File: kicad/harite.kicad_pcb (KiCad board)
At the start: 2 copper layers, 8 parts, among them J1 503480-0500, U3 Raspberry_Pi_Pico

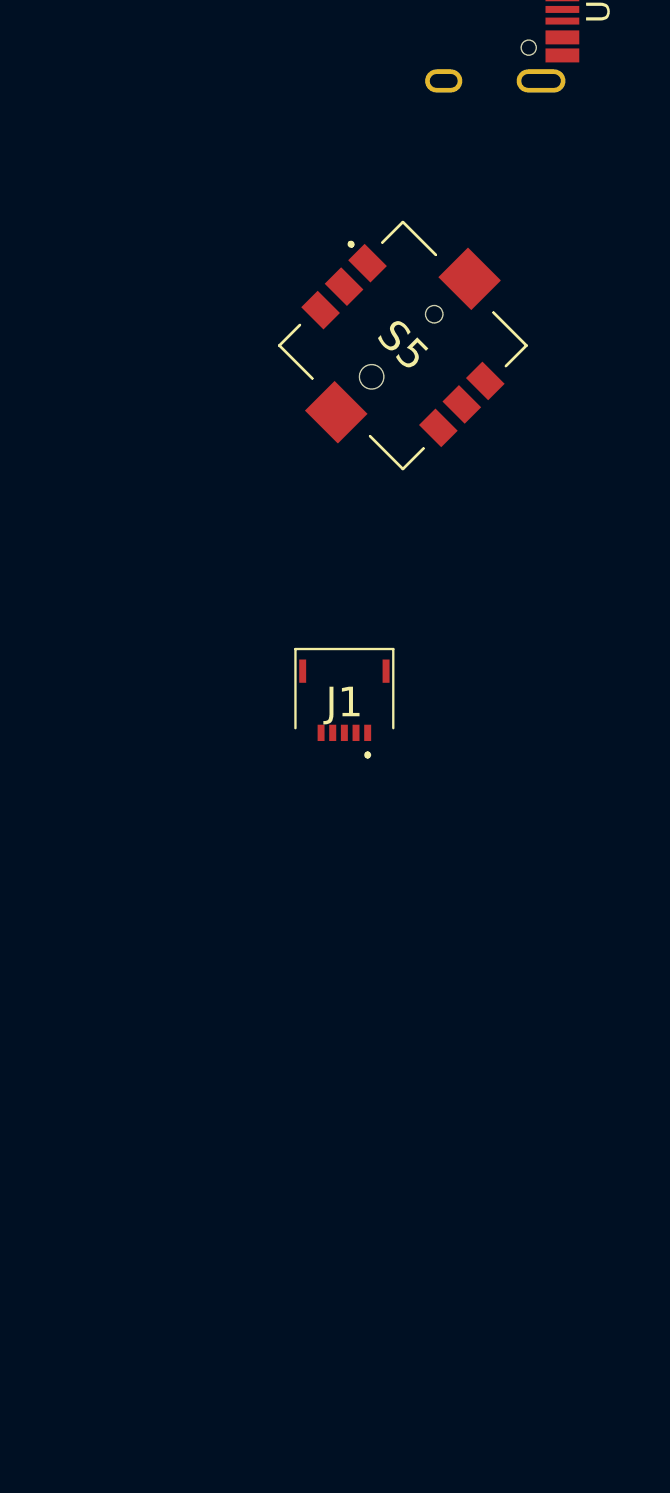
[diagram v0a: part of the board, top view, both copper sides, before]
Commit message: Add 5034800540 and 5034801000
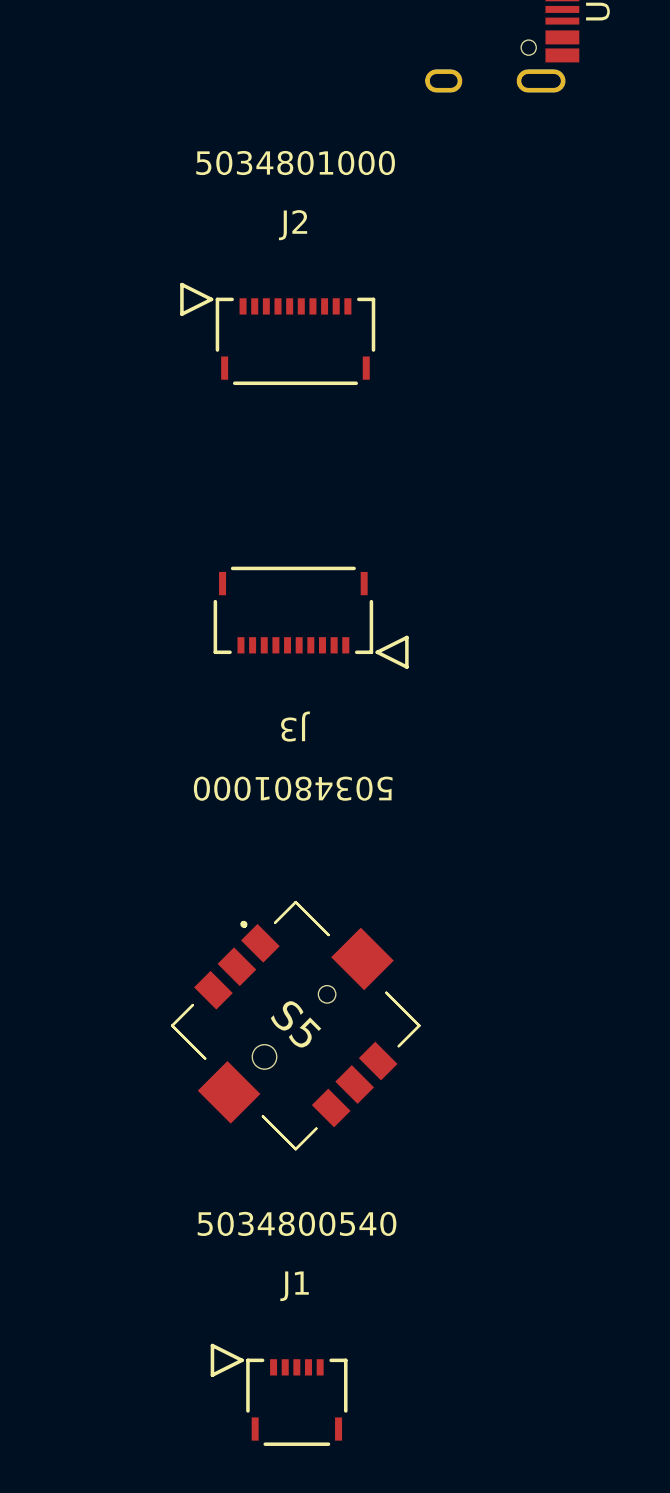
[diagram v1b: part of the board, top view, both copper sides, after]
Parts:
- added J2: 5034801000, footprints:5034801000, F.Cu at (99.2, 120.2)
- added J3: 5034801000, footprints:5034801000, F.Cu at (99.2, 131.8)
- J1: footprint footprints:5034800500 -> footprints:5034800540
- S1, S2, S3, S4, S5: footprint footprints:SKRHADE -> footprints:SKRHADE010
- moved J1 30.4 mm to (99.3, 165.8), turned to 0 degrees
- moved S5 29.6 mm to (99.3, 149.6)
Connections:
- J1 pad 1: 3V3 -> EJX
- J1 pad 2: JY -> EGND
- J1 pad 3: JC -> EJC
- J1 pad 4: GND -> EJY
- J1 pad 5: JX -> E3V3
- S5 pad 1: TN -> ETN
- S5 pad 2: TC -> ETC
- S5 pad 3: TW -> ETW
- S5 pad 4: TE -> ETE
- S5 pad 5: GND -> EGND
- S5 pad 6: TS -> ETS

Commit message: Fix model
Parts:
- J2, J3: value 5034801000 -> CON_5034801000_MOL
- moved USB1 19.4 mm to (122.4, 105.2), turned to 90 degrees
- moved J2 12.8 mm to (100.7, 107.5)
- moved J1 6.85 mm to (99.2, 158.9)
- moved U3 4.10 mm to (47.2, 119.4)
- moved S5 4.00 mm to (99.1, 145.6)
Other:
- board outline added: 100.1 x 93.3 mm

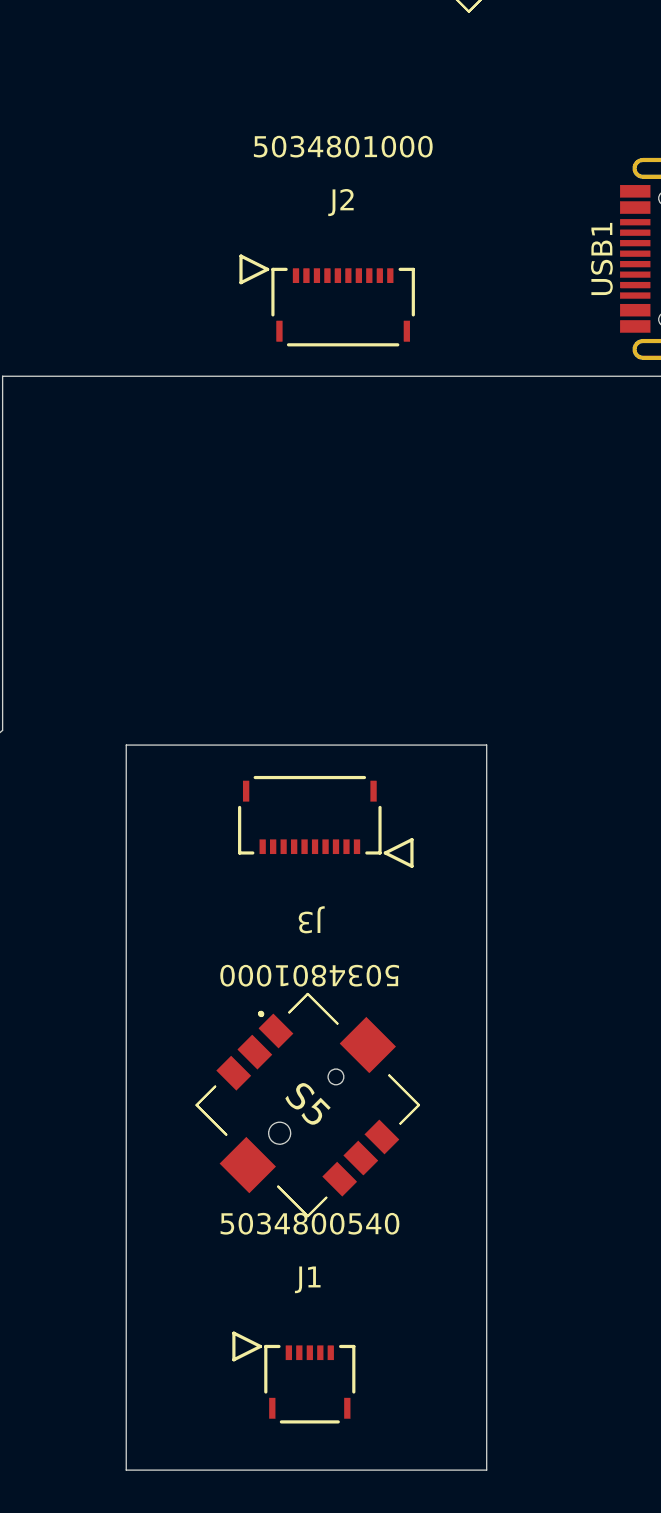
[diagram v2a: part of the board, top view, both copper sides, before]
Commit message: fix orientation
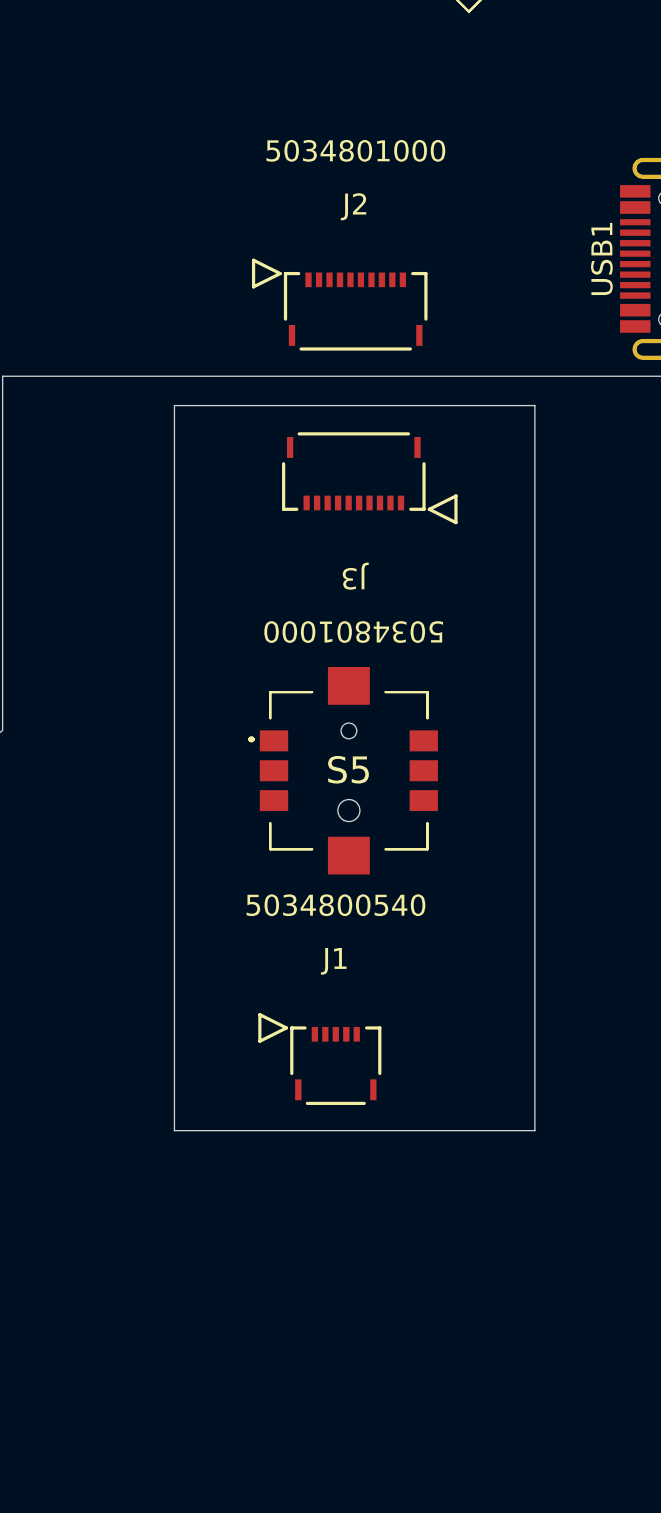
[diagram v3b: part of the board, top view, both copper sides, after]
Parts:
- J2, J3: value CON_5034801000_MOL -> 5034801000
- moved J3 16.5 mm to (101.3, 115.3)
- moved S5 16.1 mm to (101.0, 129.6), turned to 0 degrees
- moved J1 15.3 mm to (100.4, 143.7)
- moved J2 0.63 mm to (101.3, 107.7)
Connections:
- J1 pad 1: EJX -> E3V3
- J1 pad 2: EGND -> EJY
- J1 pad 4: EJY -> EGND
- J1 pad 5: E3V3 -> EJX
- J2 pad 10: GND -> TS
- J2 pad 4: JX -> GND
- J2 pad 5: TS -> JX
- J2 pad 6: TE -> TN
- J2 pad 7: TC -> TW
- J2 pad 8: TW -> TC
- J2 pad 9: TN -> TE
- J3 pad 1: EGND -> ETS
- J3 pad 2: ETN -> ETE
- J3 pad 3: ETW -> ETC
- J3 pad 4: ETC -> ETW
- J3 pad 5: ETE -> ETN
- J3 pad 6: ETS -> EJX
- J3 pad 7: EJX -> EGND
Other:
- board size 100.1 x 93.3 mm -> 100.1 x 77.1 mm

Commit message: update
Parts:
- added REF**: MountingHole_2.2mm_M2_Pad_Via, MountingHole:MountingHole_2.2mm_M2_Pad_Via, F.Cu at (68.5, 75.9)
- added REF**: MountingHole_2.2mm_M2_Pad_Via, MountingHole:MountingHole_2.2mm_M2_Pad_Via, F.Cu at (113.0, 96.2)
- added REF**: MountingHole_2.2mm_M2_Pad_Via, MountingHole:MountingHole_2.2mm_M2_Pad_Via, F.Cu at (80.0, 127.1)
- added REF**: MountingHole_2.2mm_M2_Pad_Via, MountingHole:MountingHole_2.2mm_M2_Pad_Via, F.Cu at (24.2, 102.6)
- moved J1 6.34 mm to (101.1, 137.4)
- moved S5 3.26 mm to (101.0, 126.4), turned to -45 degrees
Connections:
- S1 pad 2: unconnected-(S1-CENTER-Pad2) -> RESET
- U3 pad 30: unconnected-(U3-RUN-Pad30) -> RESET
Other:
- board size 100.1 x 77.1 mm -> 100.1 x 70.8 mm

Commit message: Switch back to rp2040 zero
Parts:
- removed J2, J3: 5034801000, footprints:5034801000
- removed REF** (x4): MountingHole_2.2mm_M2_Pad_Via, MountingHole:MountingHole_2.2mm_M2_Pad_Via
- removed U3: Raspberry_Pi_Pico, ScottoKeebs_MCU:Raspberry_Pi_Pico
- added D1: D, ScottoKeebs_Components:Diode_SOD-123, F.Cu at (27.0, 88.6)
- added D10: D, ScottoKeebs_Components:Diode_SOD-123, F.Cu at (61.2, 89.3)
- added D11: D, ScottoKeebs_Components:Diode_SOD-123, F.Cu at (77.8, 70.8)
- added D12: D, ScottoKeebs_Components:Diode_SOD-123, F.Cu at (75.8, 72.8)
- added D13: D, ScottoKeebs_Components:Diode_SOD-123, F.Cu at (73.8, 74.9)
- added D14: D, ScottoKeebs_Components:Diode_SOD-123, F.Cu at (89.5, 83.6)
- added D15: D, ScottoKeebs_Components:Diode_SOD-123, F.Cu at (86.5, 86.6)
- added D16: D, ScottoKeebs_Components:Diode_SOD-123, F.Cu at (102.2, 80.3)
- added D17: D, ScottoKeebs_Components:Diode_SOD-123, F.Cu at (100.3, 82.2)
- added D18: D, ScottoKeebs_Components:Diode_SOD-123, F.Cu at (98.6, 84.2)
- added D19: D, ScottoKeebs_Components:Diode_SOD-123, F.Cu at (114.2, 92.6)
- added D2: D, ScottoKeebs_Components:Diode_SOD-123, F.Cu at (25.0, 90.6)
- added D20: D, ScottoKeebs_Components:Diode_SOD-123, F.Cu at (111.2, 95.5)
- added D21: D, ScottoKeebs_Components:Diode_SOD-123, F.Cu at (123.5, 120.4)
- added D22: D, ScottoKeebs_Components:Diode_SOD-123, F.Cu at (121.3, 122.5)
- added D23: D, ScottoKeebs_Components:Diode_SOD-123, F.Cu at (119.1, 124.6)
- added D24: D, ScottoKeebs_Components:Diode_SOD-123, F.Cu at (134.4, 133.2)
- added D25: D, ScottoKeebs_Components:Diode_SOD-123, F.Cu at (131.3, 136.0)
- added D26: D, ScottoKeebs_Components:Diode_SOD-123, F.Cu at (257.3, 100.2)
- added D27: D, ScottoKeebs_Components:Diode_SOD-123, F.Cu at (259.3, 102.2)
- added D28: D, ScottoKeebs_Components:Diode_SOD-123, F.Cu at (261.3, 104.1)
- added D29: D, ScottoKeebs_Components:Diode_SOD-123, F.Cu at (270.1, 88.9)
- added D3: D, ScottoKeebs_Components:Diode_SOD-123, F.Cu at (23.0, 92.8)
- added D30: D, ScottoKeebs_Components:Diode_SOD-123, F.Cu at (272.9, 91.7)
- added D31: D, ScottoKeebs_Components:Diode_SOD-123, F.Cu at (232.4, 86.1)
- added D32: D, ScottoKeebs_Components:Diode_SOD-123, F.Cu at (234.5, 88.2)
- added D33: D, ScottoKeebs_Components:Diode_SOD-123, F.Cu at (236.5, 90.3)
- added D34: D, ScottoKeebs_Components:Diode_SOD-123, F.Cu at (245.2, 74.9)
- added D35: D, ScottoKeebs_Components:Diode_SOD-123, F.Cu at (248.2, 77.6)
- added D36: D, ScottoKeebs_Components:Diode_SOD-123, F.Cu at (207.4, 83.1)
- added D37: D, ScottoKeebs_Components:Diode_SOD-123, F.Cu at (209.4, 85.1)
- added D38: D, ScottoKeebs_Components:Diode_SOD-123, F.Cu at (211.5, 87.1)
- added D39: D, ScottoKeebs_Components:Diode_SOD-123, F.Cu at (220.2, 72.0)
- added D4: D, ScottoKeebs_Components:Diode_SOD-123, F.Cu at (40.0, 101.3)
- added D40: D, ScottoKeebs_Components:Diode_SOD-123, F.Cu at (223.2, 74.8)
- added D41: D, ScottoKeebs_Components:Diode_SOD-123, F.Cu at (182.4, 92.0)
- added D42: D, ScottoKeebs_Components:Diode_SOD-123, F.Cu at (184.4, 94.2)
- added D43: D, ScottoKeebs_Components:Diode_SOD-123, F.Cu at (186.5, 96.3)
- added D44: D, ScottoKeebs_Components:Diode_SOD-123, F.Cu at (162.4, 146.9)
- added D45: D, ScottoKeebs_Components:Diode_SOD-123, F.Cu at (164.5, 149.0)
- added D46: D, ScottoKeebs_Components:Diode_SOD-123, F.Cu at (166.6, 151.0)
- added D47: D, ScottoKeebs_Components:Diode_SOD-123, F.Cu at (195.1, 80.9)
- added D48: D, ScottoKeebs_Components:Diode_SOD-123, F.Cu at (197.8, 83.7)
- added D49: D, ScottoKeebs_Components:Diode_SOD-123, F.Cu at (174.7, 135.6)
- added D5: D, ScottoKeebs_Components:Diode_SOD-123, F.Cu at (36.5, 104.3)
- added D50: D, ScottoKeebs_Components:Diode_SOD-123, F.Cu at (177.8, 138.5)
- added D6: D, ScottoKeebs_Components:Diode_SOD-123, F.Cu at (52.2, 74.3)
- added D7: D, ScottoKeebs_Components:Diode_SOD-123, F.Cu at (50.2, 76.3)
- added D8: D, ScottoKeebs_Components:Diode_SOD-123, F.Cu at (48.2, 78.3)
- added D9: D, ScottoKeebs_Components:Diode_SOD-123, F.Cu at (64.4, 86.8)
- added G***: LOGO, footprints:logo-right, F.Cu at (175.2, 115.3)
- added G***: LOGO, footprints:logo-left, F.Cu at (47.2, 90.5)
- added H1: Mounting_Hole, MountingHole:MountingHole_2.2mm_M2_Pad_Via, F.Cu at (23.6, 103.2)
- added H10: Mounting_Hole, MountingHole:MountingHole_2.2mm_M2_Pad_Via, F.Cu at (168.6, 126.8)
- added H2: Mounting_Hole, MountingHole:MountingHole_2.2mm_M2_Pad_Via, F.Cu at (36.4, 78.8)
- added H3: Mounting_Hole, MountingHole:MountingHole_2.2mm_M2_Pad_Via, F.Cu at (69.3, 80.8)
- added H4: Mounting_Hole, MountingHole:MountingHole_2.2mm_M2_Pad_Via, F.Cu at (118.5, 83.5)
- added H5: Mounting_Hole, MountingHole:MountingHole_2.2mm_M2_Pad_Via, F.Cu at (94.9, 75.5)
- added H6: Mounting_Hole, MountingHole:MountingHole_2.2mm_M2_Pad_Via, F.Cu at (273.6, 103.2)
- added H7: Mounting_Hole, MountingHole:MountingHole_2.2mm_M2_Pad_Via, F.Cu at (260.9, 78.8)
- added H8: Mounting_Hole, MountingHole:MountingHole_2.2mm_M2_Pad_Via, F.Cu at (227.9, 80.8)
- added H9: Mounting_Hole, MountingHole:MountingHole_2.2mm_M2_Pad_Via, F.Cu at (178.8, 83.5)
- added J4: CON_5034801200_MOL, footprints:5034801200, F.Cu at (126.7, 111.5)
- added J5: CON_5034801200_MOL, footprints:5034801200, F.Cu at (126.7, 97.1)
- added S10: SKRHADE010, footprints:SKRHADE, F.Cu at (170.4, 143.1)
- added S6: SKRHADE010, footprints:SKRHADE, F.Cu at (265.4, 96.1)
- added S7: SKRHADE010, footprints:SKRHADE, F.Cu at (240.4, 82.1)
- added S8: SKRHADE010, footprints:SKRHADE, F.Cu at (215.4, 79.1)
- added S9: SKRHADE010, footprints:SKRHADE, F.Cu at (190.4, 88.1)
- added U1: RP2040_Zero, ScottoKeebs_MCU:RP2040_Zero, F.Cu at (133.0, 72.8)
- added U2: RP2040_Zero, ScottoKeebs_MCU:RP2040_Zero, F.Cu at (164.2, 81.8)
- added USB2: HRO-TYPE-C-31-M-12, footprints:HRO-TYPE-C-31-M-12, F.Cu at (151.6, 113.3)
- S1, S2, S3, S4, S5: footprint footprints:SKRHADE010 -> footprints:SKRHADE
- moved USB1 26.8 mm to (145.4, 91.4)
- moved J1 26.4 mm to (126.6, 144.2)
- moved S5 25.9 mm to (126.8, 129.0)
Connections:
- S1 pad 1: PN -> Net-(D1-A)
- S1 pad 2: RESET -> Net-(D2-A)
- S1 pad 3: PW -> Net-(D3-A)
- S1 pad 4: PE -> Net-(D4-A)
- S1 pad 5: GND -> Col 1
- S1 pad 6: PS -> Net-(D5-A)
- S2 pad 1: RN -> Net-(D6-A)
- S2 pad 2: unconnected-(S2-CENTER-Pad2) -> Net-(D7-A)
- S2 pad 3: RW -> Net-(D8-A)
- S2 pad 4: RE -> Net-(D9-A)
- S2 pad 5: GND -> Col 2
- S2 pad 6: RS -> Net-(D10-A)
- S3 pad 1: MN -> Net-(D11-A)
- S3 pad 2: unconnected-(S3-CENTER-Pad2) -> Net-(D12-A)
- S3 pad 3: MW -> Net-(D13-A)
- S3 pad 4: ME -> Net-(D14-A)
- S3 pad 5: GND -> Col 3
- S3 pad 6: MS -> Net-(D15-A)
- S4 pad 1: IN -> Net-(D16-A)
- S4 pad 2: unconnected-(S4-CENTER-Pad2) -> Net-(D17-A)
- S4 pad 3: IW -> Net-(D18-A)
- S4 pad 4: IE -> Net-(D19-A)
- S4 pad 5: GND -> Col 4
- S4 pad 6: IS -> Net-(D20-A)
- S5 pad 1: ETN -> Net-(D21-A)
- S5 pad 2: ETC -> Net-(D22-A)
- S5 pad 3: ETW -> Net-(D23-A)
- S5 pad 4: ETE -> Net-(D24-A)
- S5 pad 5: EGND -> ECol 5
- S5 pad 6: ETS -> Net-(D25-A)
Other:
- board size 100.1 x 70.8 mm -> 258.2 x 95.8 mm
- board text added: "Cirque"
- board text added: "GND"
- board text added: "SCK"
- board text added: "SI"
- board text added: "SO"
- board text added: "SS"
- board text added: "VDD"

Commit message: update
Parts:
- added J2: Wired Joystick, footprints:Wired-Joystick, F.Cu at (127.6, 132.8)
- J4, J5: value CON_5034801200_MOL -> 5034801200
- moved G*** 69.5 mm to (114.0, 71.3)
- moved D23 6.68 mm to (122.2, 118.7)
- moved D25 6.53 mm to (134.1, 130.2)
- moved S5 6.53 mm to (129.6, 123.2)
- moved D22 6.53 mm to (124.1, 116.7)
- moved D21 6.53 mm to (126.4, 114.6)
- moved D24 6.35 mm to (137.1, 127.4)
- moved J1 5.94 mm to (129.5, 139.0)
- moved J4 4.75 mm to (129.7, 107.9)
- moved J5 3.05 mm to (129.8, 97.2)
- moved USB1 1.59 mm to (147.0, 91.4)
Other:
- outline, holes or cut-outs redrawn

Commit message: add joycon
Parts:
- moved H10 72.9 mm to (160.3, 54.3)
- moved H5 65.3 mm to (122.2, 134.8)
- moved H2 59.4 mm to (94.8, 68.4)
- moved H3 53.4 mm to (120.2, 97.2)
- moved H9 39.7 mm to (160.3, 48.4)
- moved H4 37.6 mm to (141.5, 113.2)
- moved J2 15.6 mm to (140.7, 124.4), turned to 90 degrees
- moved J1 12.1 mm to (140.7, 134.4)
- moved D25 11.0 mm to (136.1, 119.3), turned to -45 degrees
- moved D24 6.85 mm to (134.0, 121.4), turned to -45 degrees
- moved J4 5.74 mm to (129.6, 113.6)
- moved D22 5.17 mm to (124.1, 121.8)
- moved D23 5.17 mm to (122.2, 123.8)
- moved D21 5.17 mm to (126.4, 119.7)
- moved S5 5.04 mm to (129.6, 128.2)
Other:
- outline, holes or cut-outs redrawn
